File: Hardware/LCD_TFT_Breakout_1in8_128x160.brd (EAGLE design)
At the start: 43.2 x 59.9 mm, 55 parts, among them Q1 220mA/50V/3.5Ω, Q2 220mA/50V/3.5Ω, U2 W25Q32FV, U6 TXB0108DQSR, U7 3.3V

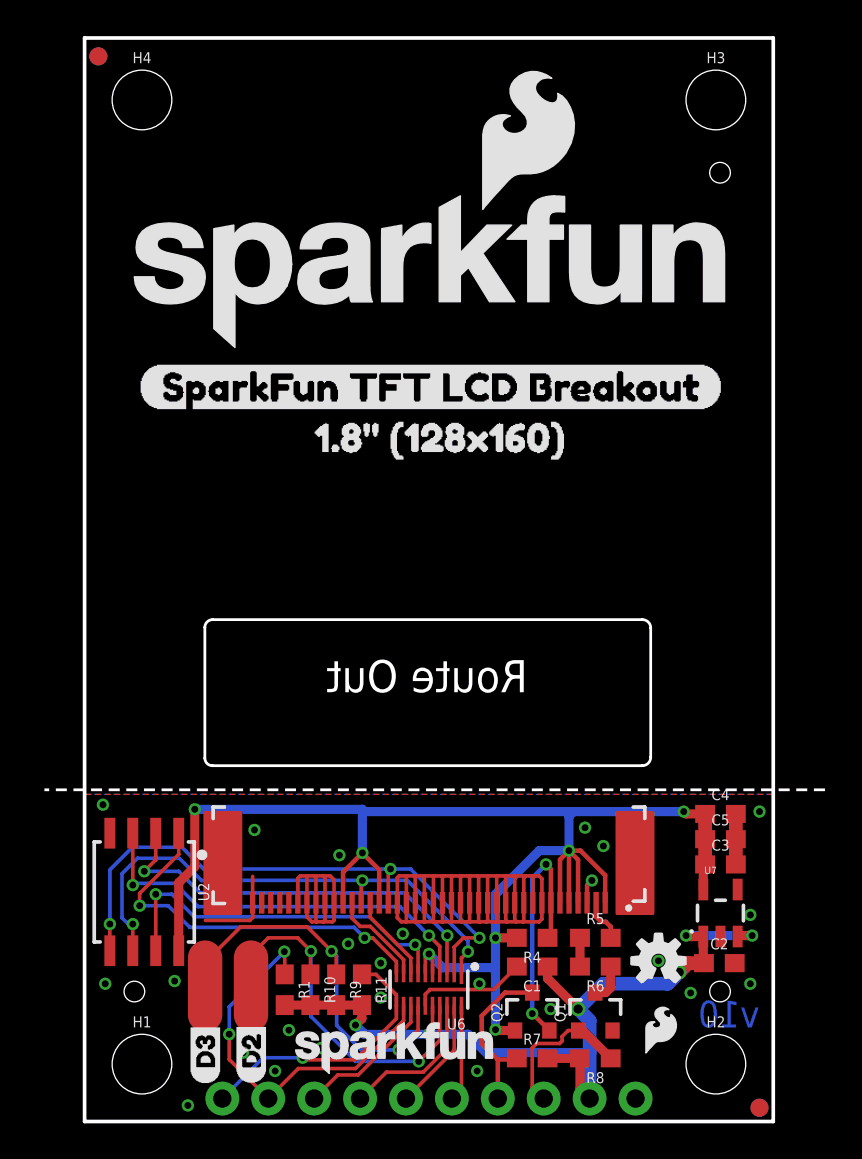
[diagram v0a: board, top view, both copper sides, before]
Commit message: Change to SD from SPI flash
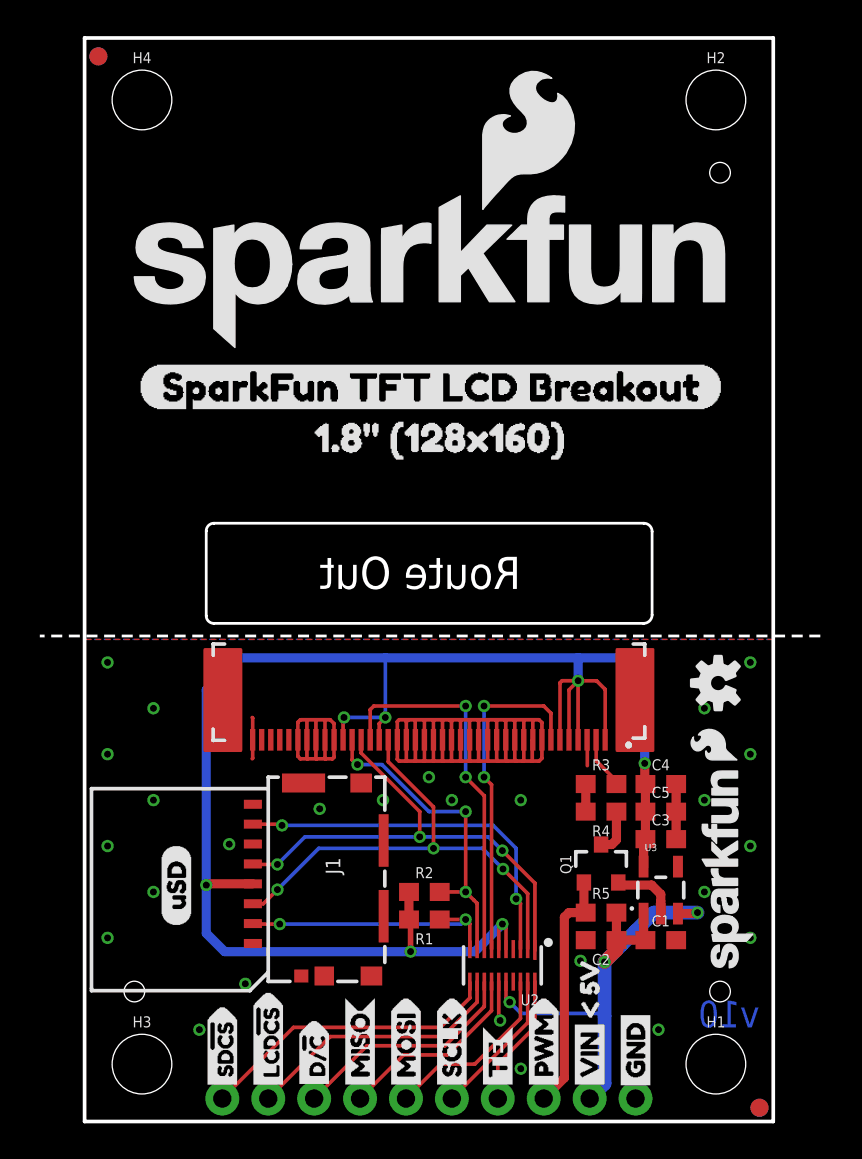
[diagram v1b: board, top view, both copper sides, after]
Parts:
- removed J3: (no value), 1in8_breakout:1X02_USER_SMD
- removed Q2: 220mA/50V/3.5Ω, SparkFun-DiscreteSemi:SOT23-3
- removed R10, R11, R7, R8, R9: 10k, SparkFun-Resistors:0603
- removed R6: 1, SparkFun-Resistors:0603
- removed U6: TXB0108DQSR, SparkFun-IC-Comms:UFDFN-20
- removed U7: 3.3V, SparkFun-IC-Power:SOT23-5
- added J2: (no value), SparkFun-Connectors:1X10_NO_SILK
- added LOGO3: OSHW-LOGOS, SparkFun-Aesthetics:OSHW-LOGO-S
- added R2: 10k, SparkFun-Resistors:0603
- added R3: 1, SparkFun-Resistors:0603
- added U$17: (no value), cs:#_5V_4
- added U$25: (no value), buzzard_labels:D##C7
- added U$26: (no value), buzzard_labels:MISO3
- added U$27: (no value), buzzard_labels:MOSI2
- added U$28: (no value), buzzard_labels:SCLK4
- added U$29: (no value), buzzard_labels:TE5
- added U$30: (no value), buzzard_labels:PWM6
- added U$31: (no value), buzzard_labels:VIN1
- added U$32: (no value), buzzard_labels:GND0
- added U3: 3.3V, SparkFun-IC-Power:SOT23-5
- C1: value 0.1uF -> 1.0uF
- C2: value 1.0uF -> 0.1uF
- J1: value (none) -> MICRO-SD_CARD_SOCKETTINY; device SparkFun-Connectors:1X10_NO_SILK -> SparkFun-Connectors:MICROSD_TINY
- LOGO2: value OSHW-LOGOS -> SPECIAL_INSTRUCTIONS-PRODUCTION; device SparkFun-Aesthetics:OSHW-LOGO-S -> SparkFun-Aesthetics:PRODUCTION_INSTRUCTIONS
- R4: value 10k -> 1
- R5: value 1 -> 10k
- U$16: device buzzard_labels:S#CS9 -> cs:SD#CS0
- U$4: value SPECIAL_INSTRUCTIONS-PRODUCTION -> (none); device SparkFun-Aesthetics:PRODUCTION_INSTRUCTIONS -> cs:USD2
- U$5: device buzzard_labels:D210 -> cs:LCD#CS1
- U$6: device buzzard_labels:D311 -> cs:LCD#CS1
- U$8: device buzzard_labels:F#CS8 -> cs:SD#CS0
- U2: value W25Q32FV -> TXB0108DQSR; device SparkFun-IC-Memory:SOIC-8 -> SparkFun-IC-Comms:UFDFN-20
- moved LOGO2 136.5 mm to (-100.7, -23.9)
- moved U$4 111.3 mm to (5.08, 10.8), turned to 90 degrees
- moved H3 62.1 mm to (3.17, 3.17)
- moved H2 53.3 mm to (34.9, 56.5)
- moved H1 31.7 mm to (34.9, 3.17)
- moved J1 27.0 mm to (10.2, 19.1), flipped to the top, turned to 270 degrees
- moved U$2 20.9 mm to (35.6, 14.0), turned to 90 degrees
- moved U2 20.2 mm to (23.1, 8.64)
- moved U$3 16.0 mm to (34.8, 20.8), turned to 90 degrees
- moved U1 9.02 mm to (19.1, 21.7)
- moved U$23 8.89 mm to (31.9, 25.5)
- moved U$24 8.89 mm to (26.3, 23.0)
- moved R1 8.64 mm to (18.8, 11.2), turned to 180 degrees
- moved Q1 8.20 mm to (28.6, 14.2)
- moved R4 7.96 mm to (28.6, 17.1)
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- renumbered FRAME2 to FRAME1
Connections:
- removed net D2: U2.3, U6.4
- removed net D2_IN: J3.1, R10.1, U6.17
- removed net D3: U2.7, U6.7
- removed net D3_IN: J3.2, R9.1, U6.14
- removed net FLASH_!CS: U2.1, U6.10
- removed net FLASH_!CS!_IN: J1.10, R11.1, U6.11
- new net SD_!CS: J1.2, R1.1, U2.10
- new net SD_!CS!_IN: J2.10, U2.11
- net !CS: now also R2.2, U2.9; no longer U6.9
- net !CS!_IN: now also J2.9, U2.12; no longer J1.9, R1.1, U6.12
- net 3.3V: now also J1.4, R1.2, R2.1, U2.5, U2.6, U3.5; no longer Q2.1, R4.2, U2.8, U6.5, U6.6, U7.5
- net D/!C: now also U2.8; no longer U6.8
- net D/!C!_IN: now also J2.8, U2.13; no longer J1.8, U6.13
- net GND: now also J1.6, J2.1, U2.15, U3.2; no longer J1.1, U2.4, U6.15, U7.2
- net LEDK: now also R3.2; no longer R5.2
- net LED_PWM: now also J2.3, R5.1; no longer J1.3, R8.1
- net MISO: now also J1.7, U2.3; no longer U2.2, U6.3
- net MISO_IN: now also J2.6, U2.18; no longer J1.7, U6.18
- net MOSI: now also J1.3, U2.2; no longer U2.5, U6.2
- net MOSI_IN: now also J2.5, U2.19; no longer J1.6, U6.19
- net N$4: now also R3.1, R4.2; no longer R5.1, R6.2
- net N$5: now also R4.1; no longer R6.1
- net SCLK: now also J1.5, U2.1; no longer U2.6, U6.1
- net SCLK_IN: now also J2.4, U2.20; no longer J1.5, U6.20
- net TE: now also U2.7; no longer Q2.2, R4.1
- net TE_IN: now also J2.7, U2.14; no longer J1.4, Q2.3, R7.1
- net VIN: now also J2.2, R5.2, U2.16, U3.1, U3.3; no longer J1.2, R1.2, R10.2, R11.2, R7.2, R8.2, R9.2, U6.16, U7.1, U7.3
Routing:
- net D2: track 22.8 -> 0.00 mm, vias 2 -> 0
- net D3_IN: track 22.2 -> 0.00 mm, vias 2 -> 0
- net D2_IN: track 21.5 -> 0.00 mm, vias 2 -> 0
- net FLASH_!CS: track 21.0 -> 0.00 mm, vias 2 -> 0
- net D3: track 20.3 -> 0.00 mm, vias 2 -> 0
- net VIN: track 48.2 -> 28.2 mm, vias 6 -> 3
- net SD_!CS!_IN: track 0.00 -> 16.9 mm
- net D/!C: track 4.83 -> 20.9 mm, vias 0 -> 2
- net FLASH_!CS!_IN: track 15.2 -> 0.00 mm, vias 1 -> 0
- net SD_!CS: track 0.00 -> 15.1 mm, vias 0 -> 2
- net 3.3V: track 86.0 -> 100.7 mm
- net !CS: track 5.41 -> 17.9 mm, vias 0 -> 3
- net !CS!_IN: track 21.6 -> 14.9 mm, vias 2 -> 0
- net GND: track 88.5 -> 82.3 mm, vias 23 -> 25
- net LED_PWM: track 8.59 -> 13.5 mm
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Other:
- outline, holes or cut-outs redrawn

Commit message: Small fixes/tweaks according to checklist
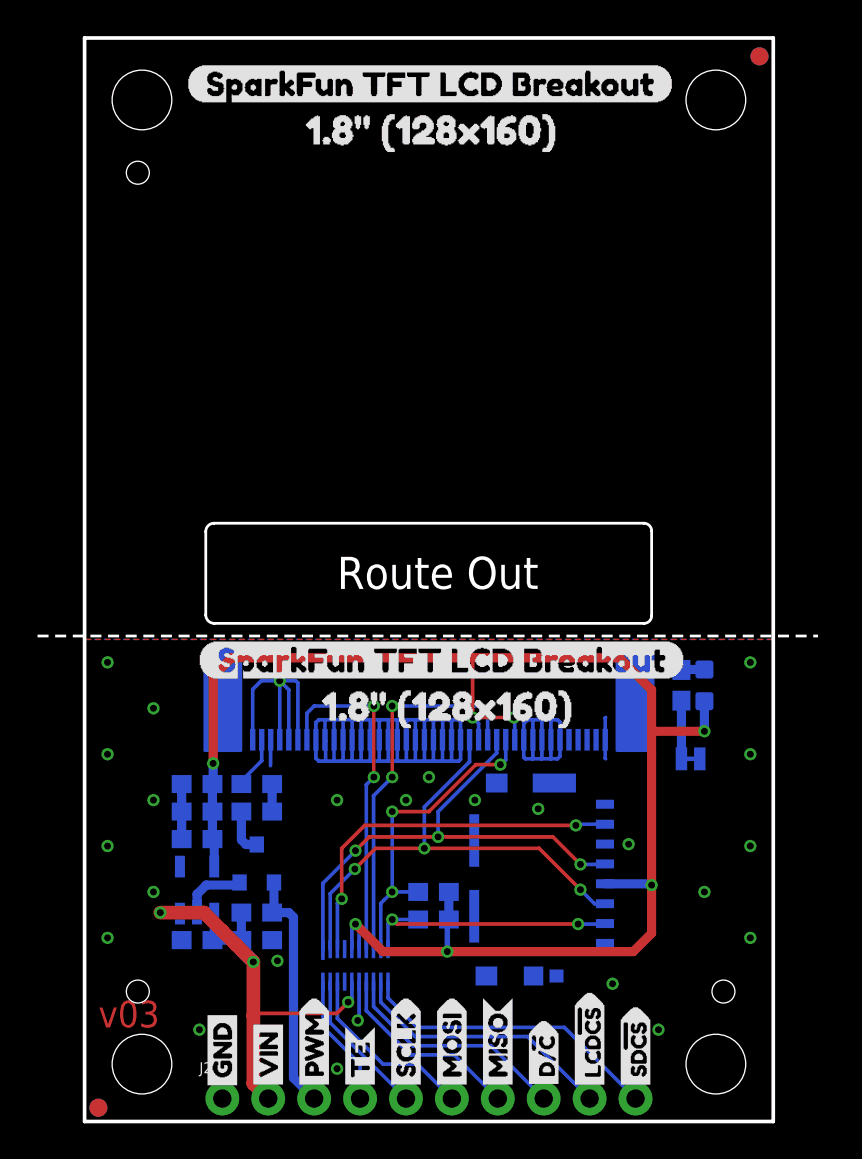
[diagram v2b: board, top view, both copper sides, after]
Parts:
- removed U$1: (no value), 1in8_breakout:KWH018ST14-F01_HOLES
- added D1: RED, SparkFun-LED:LED-0603
- added JP1: LED, SparkFun-Jumpers:SMT-JUMPER_2_NC_TRACE_SILK
- added R6: 1k, SparkFun-Resistors:0603
- added U$18: (no value), cs:PWR4
- added U$33: EXTERNAL_DISP-KWH018ST14-F01, SparkFun-Displays:KWH018ST14-F01_HOLES
- U1: device 1in8_breakout:FPC05040-17204 -> SparkFun-Displays:FPC05040-17204
- moved LOGO2 239.5 mm to (138.8, -23.9), flipped to the bottom
- moved FRAME1 198.1 mm to (118.1, 1.27), flipped to the bottom
- moved FD1 36.6 mm to (37.3, 58.9), flipped to the bottom
- moved FD2 36.6 mm to (0.76, 0.76), flipped to the bottom
- moved FD3 36.6 mm to (37.3, 58.9), flipped to the top
- moved FD4 36.6 mm to (0.76, 0.76), flipped to the top
- moved U$2 33.0 mm to (2.54, 14.0), flipped to the bottom
- moved U$19 32.3 mm to (35.2, 40.6), flipped to the bottom
- moved LOGO3 32.0 mm to (3.05, 24.3), flipped to the bottom
- moved H1 31.7 mm to (3.17, 3.17), flipped to the bottom
- moved H2 31.7 mm to (3.17, 56.5), flipped to the bottom
- moved H3 31.7 mm to (34.9, 3.17), flipped to the bottom
- moved H4 31.7 mm to (34.9, 56.5), flipped to the bottom
- moved U$3 31.5 mm to (3.30, 20.8), flipped to the bottom
- moved U$4 27.9 mm to (33.0, 10.8), flipped to the bottom
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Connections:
- new net N$1: D1.C, R6.2
- new net N$2: JP1.2, R6.1
- net 3.3V: now also D1.A
- net GND: now also JP1.1
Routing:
- net 3.3V: track 100.7 -> 105.3 mm, vias 7 -> 8
- net N$2: track 0.00 -> 3.21 mm
- net N$1: track 0.00 -> 1.28 mm
- net GND: vias 25 -> 23
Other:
- outline, holes or cut-outs redrawn
- board text added: "IN"
- board text added: "MM"
- board text added: "v03"
- board text removed: "v10"

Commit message: Improve ground plane continuity
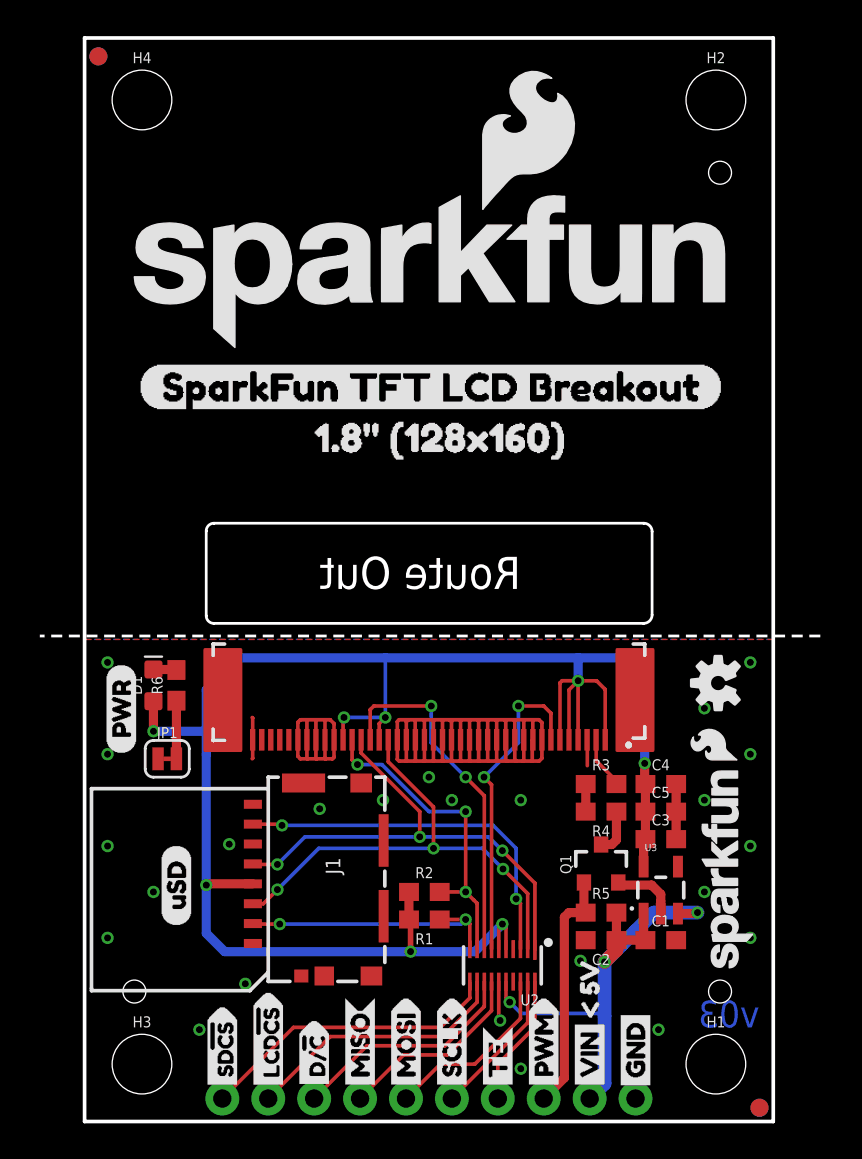
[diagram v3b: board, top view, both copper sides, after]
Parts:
- moved LOGO2 148.1 mm to (-9.14, -29.6), flipped to the top, turned to 90 degrees
- moved FRAME1 99.5 mm to (19.1, -7.62), flipped to the top, turned to 90 degrees
- moved FD1 36.6 mm to (0.76, 58.9), flipped to the top
- moved FD2 36.6 mm to (37.3, 0.76), flipped to the top
- moved FD3 36.6 mm to (0.76, 58.9), flipped to the bottom
- moved FD4 36.6 mm to (37.3, 0.76), flipped to the bottom
- moved U$33 34.3 mm to (1.91, 53.3), flipped to the bottom
- moved U$18 34.0 mm to (2.03, 20.3), flipped to the top
- moved U$2 33.0 mm to (35.6, 14.0), flipped to the top
- moved U$19 32.3 mm to (2.92, 40.6), flipped to the top
- moved LOGO3 32.0 mm to (35.1, 24.3), flipped to the top
- moved H1 31.7 mm to (34.9, 3.17), flipped to the top
- moved H2 31.7 mm to (34.9, 56.5), flipped to the top
- moved H3 31.7 mm to (3.17, 3.17), flipped to the top
- moved H4 31.7 mm to (3.17, 56.5), flipped to the top
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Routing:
- net D/!C: track 20.9 -> 19.8 mm
- net TE: track 19.0 -> 17.8 mm
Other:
- outline, holes or cut-outs redrawn

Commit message: Perform Proto Review task items
Completes and closes issue #1
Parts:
- removed U$17: (no value), cs:#_5V_4
- removed U$31: (no value), buzzard_labels:VIN1
- added U$1: (no value), V3to5:3V3#5V50
- moved FRAME1 24.6 mm to (0.00, -23.1), turned to 0 degrees
- moved LOGO2 18.8 mm to (-24.5, -40.4), turned to 0 degrees
- moved U$4 3.43 mm to (1.65, 10.8)
- moved J1 2.54 mm to (7.62, 19.1)
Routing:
- net SCLK: track 27.7 -> 30.3 mm
- net MOSI: track 27.6 -> 30.2 mm
- net SD_!CS: track 15.1 -> 17.6 mm
- net MISO: track 20.8 -> 23.3 mm
- net 3.3V: track 105.3 -> 104.6 mm
- net GND: vias 23 -> 30
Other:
- board size 43.2 x 59.9 mm -> 42.8 x 59.9 mm

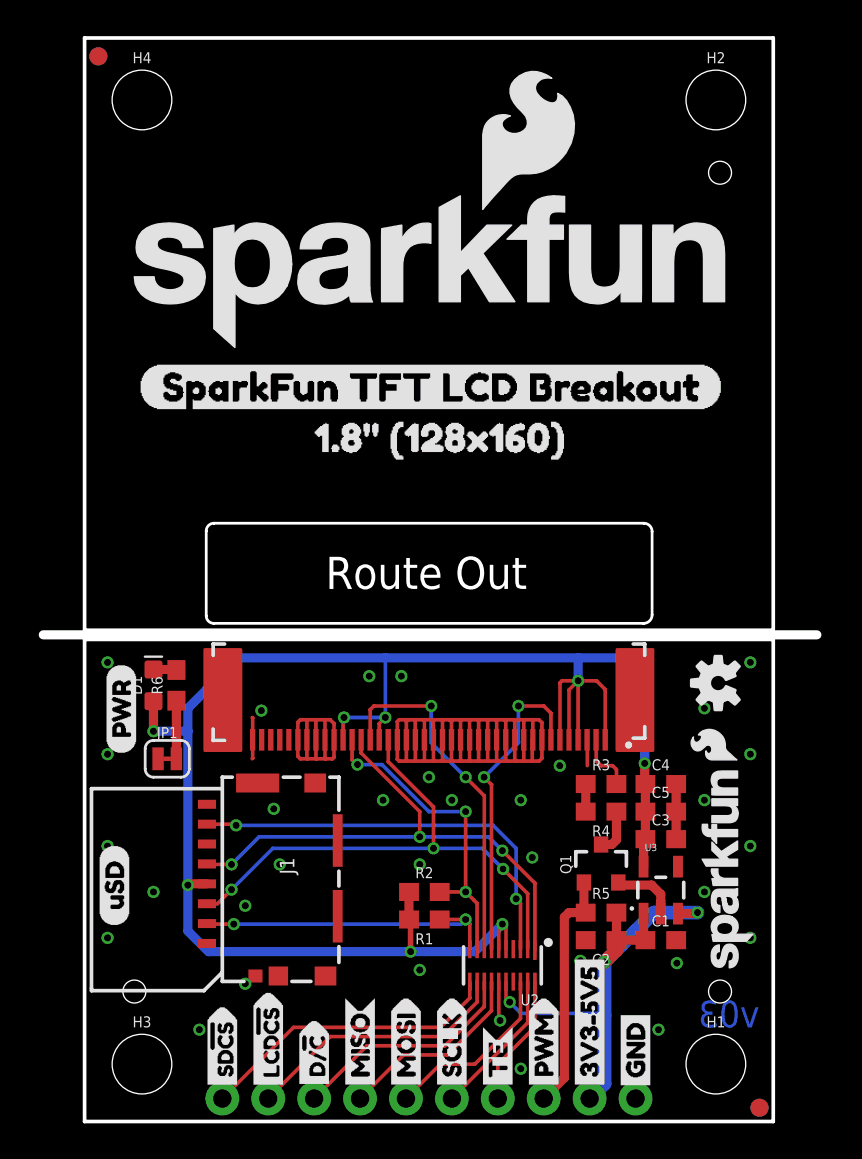
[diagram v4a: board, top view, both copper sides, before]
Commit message: Perform checklist after proto review
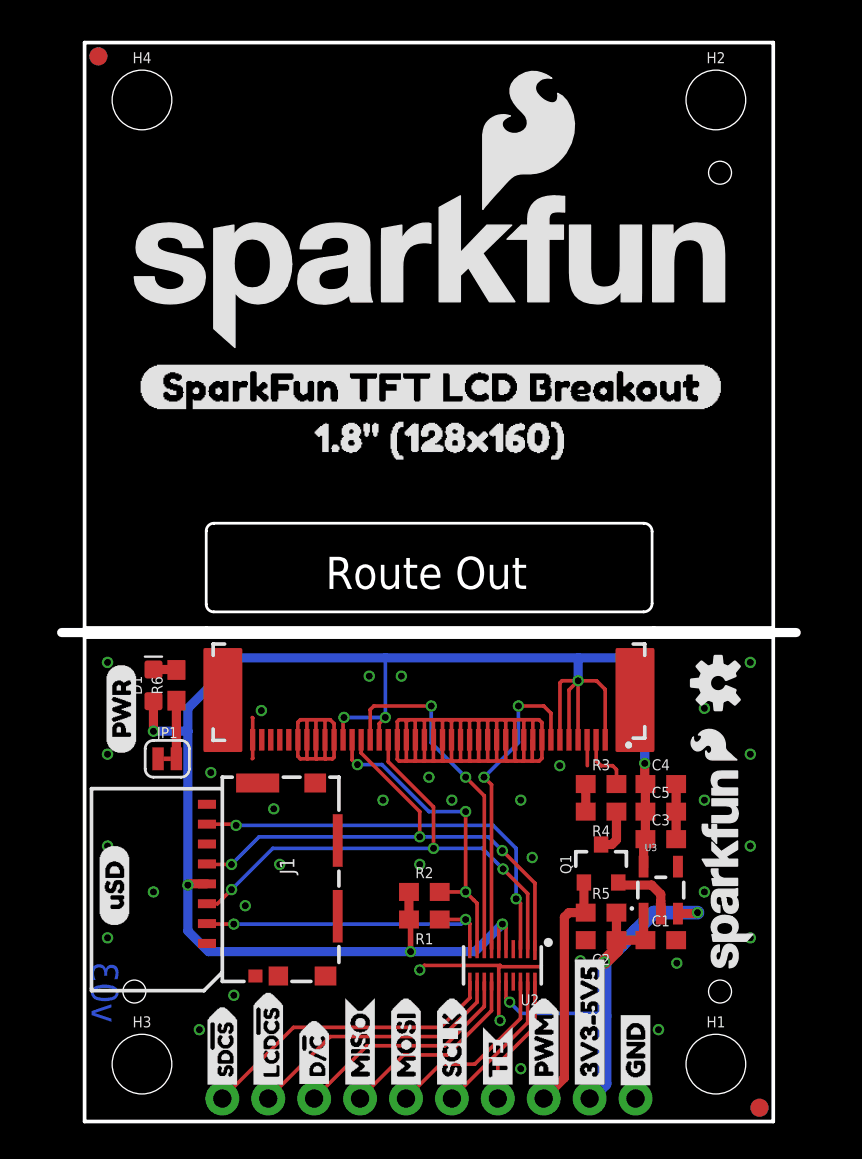
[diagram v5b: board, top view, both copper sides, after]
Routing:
- net GND: track 82.3 -> 90.1 mm, vias 30 -> 31
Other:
- board size 42.8 x 59.9 mm -> 40.6 x 59.7 mm
- board text removed: "MM"
